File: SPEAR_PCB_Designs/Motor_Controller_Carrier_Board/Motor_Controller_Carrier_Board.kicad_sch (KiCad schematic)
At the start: 0 parts

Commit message: Added symbol for motor driver board and started the schematic
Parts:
- added F1, F2: Fuse, symbol Device:Fuse
- added J1, J2, J3: Conn_01x02_Pin, symbol Connector:Conn_01x02_Pin
- added MDB1: Motor_Driver_Board, Motor_Controller_Carrier_Board:Motor_Driver_Board, symbol Motor_Controller_Carrier_Board:Motor_Driver_Board
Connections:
- new net: J2.1 (Pin_1), MDB1.13 (OUTA), MDB1.14 (OUTA)
- new net: J2.2 (Pin_2), MDB1.11 (OUTB), MDB1.12 (OUTB)
- new net: J1.1 (Pin_1), J3.1 (Pin_1), MDB1.1 (GND), MDB1.10 (GND), MDB1.9 (GND)
- new net: F1.2, F2.1, J1.2 (Pin_2)
- new net: F2.2, MDB1.15 (VIN), MDB1.16 (VIN)
- new net: F1.1, J3.2 (Pin_2)

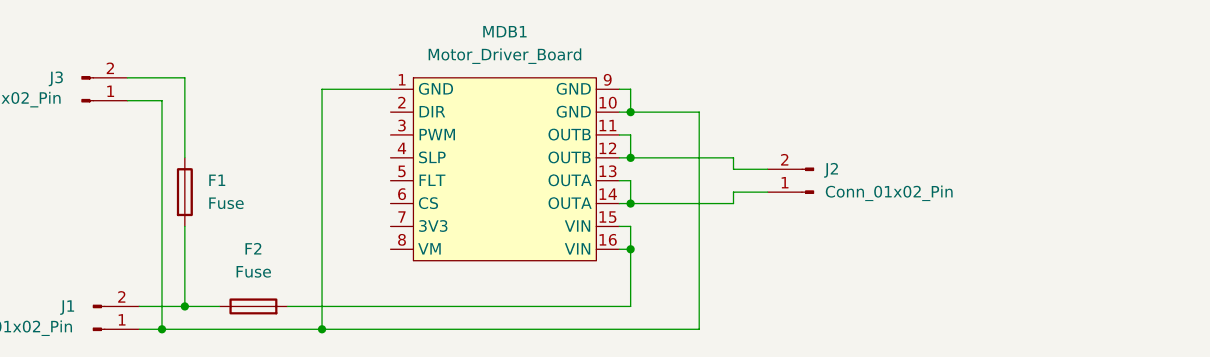
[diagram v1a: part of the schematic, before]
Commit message: Started Carrier Board PCB layout
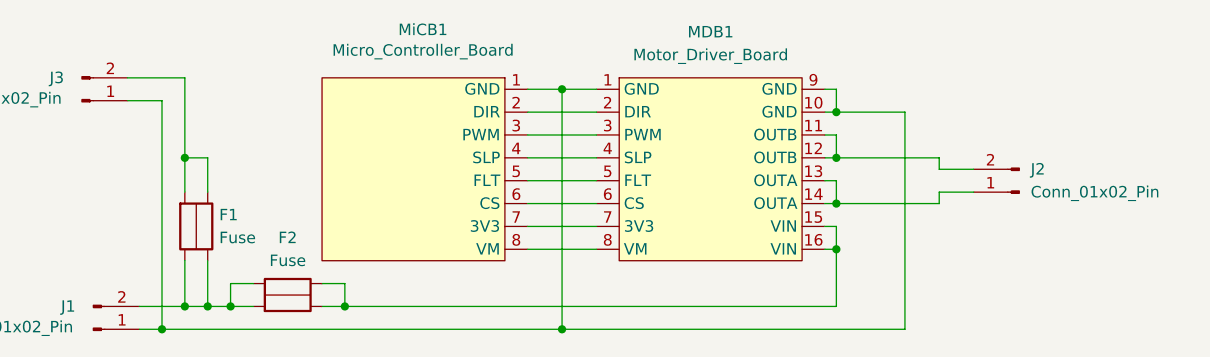
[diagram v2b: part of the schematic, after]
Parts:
- removed F1, F2: Fuse, symbol Device:Fuse
- added F1, F2: Fuse, Motor_Controller_Carrier_Board:Fuse, symbol Motor_Controller_Carrier_Board:Fuse
- added MiCB1: Micro_Controller_Board, Motor_Controller_Carrier_Board:Micro_Controller_Board, symbol Motor_Controller_Carrier_Board:Micro_Controller_Board
- J1, J2, J3: footprint (none) -> XT30:AMASS_XT30PW-M
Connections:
- net at J1.1 (Pin_1), J3.1 (Pin_1), MDB1.1 (GND)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: now also MiCB1.1 (GND)
- net at J1.2 (Pin_2): now also F1.2, F1.4, F2.1, F2.3
- net at MDB1.15 (VIN), MDB1.16 (VIN): now also F2.2, F2.4
- net at MDB1.2 (DIR): now also MiCB1.2 (DIR)
- net at MDB1.3 (PWM): now also MiCB1.3 (PWM)
- net at MDB1.4 (SLP): now also MiCB1.4 (SLP)
- net at MDB1.5 (FLT): now also MiCB1.5 (FLT)
- net at MDB1.6 (CS): now also MiCB1.6 (CS)
- net at MDB1.7 (3V3): now also MiCB1.7 (3V3)
- net at MDB1.8 (VM): now also MiCB1.8 (VM)
- net at J3.2 (Pin_2): now also F1.1, F1.3
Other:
- moved on the sheet: J2, MDB1

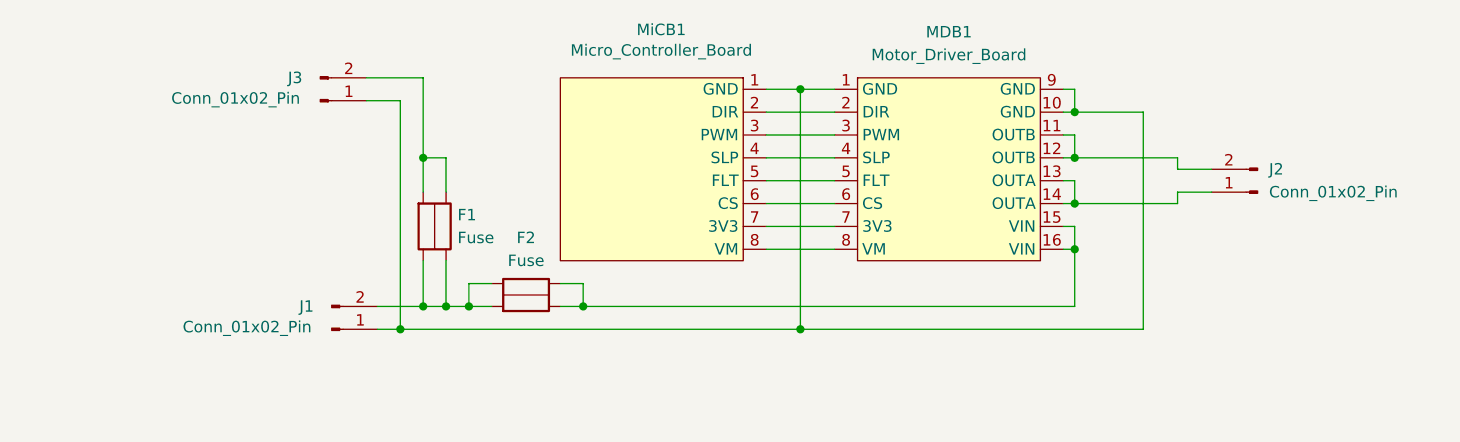
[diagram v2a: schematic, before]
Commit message: added Carrier Board PCB
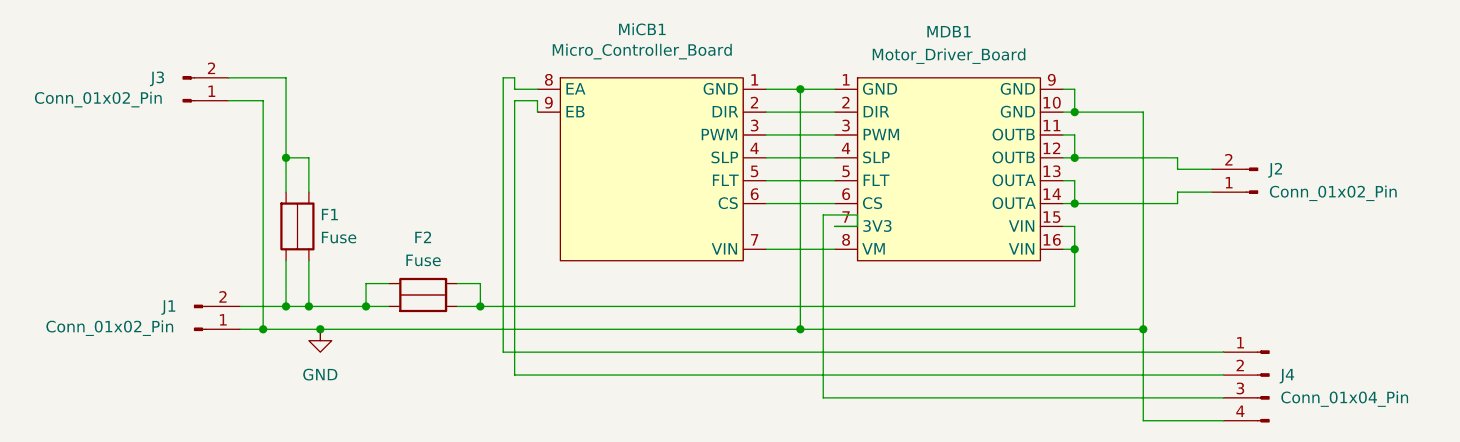
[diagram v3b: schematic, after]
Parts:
- added J4: Conn_01x04_Pin, Motor_Controller_Carrier_Board:JST_GH_BM04B-GHS-TBT_1x04-1MP_P1.25mm_Vertical, symbol Connector:Conn_01x04_Pin
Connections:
- net GND: now reaches J1.1 (Pin_1), J3.1 (Pin_1), MDB1.1 (GND), MDB1.10 (GND), MDB1.9 (GND), MiCB1.1 (GND)
- net GND: now also J4.4 (Pin_4)
- net at MiCB1.7 (VIN): now also MDB1.8 (VM); no longer MDB1.7 (3V3)
- net at MiCB1.8 (EA): now also J4.1 (Pin_1); no longer MDB1.8 (VM)
- new net: J4.2 (Pin_2), MiCB1.9 (EB)
- new net: J4.3 (Pin_3), MDB1.7 (3V3)
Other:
- moved on the sheet: F1, F2, J1, J3

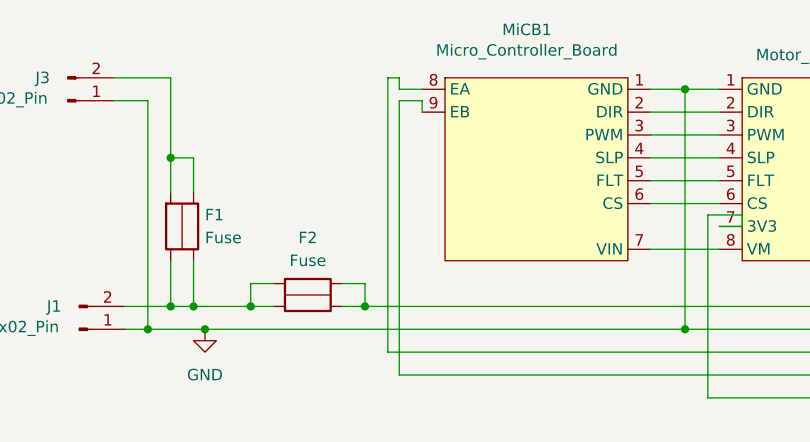
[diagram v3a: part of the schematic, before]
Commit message: moved board footprints and created new motor driver board footprints
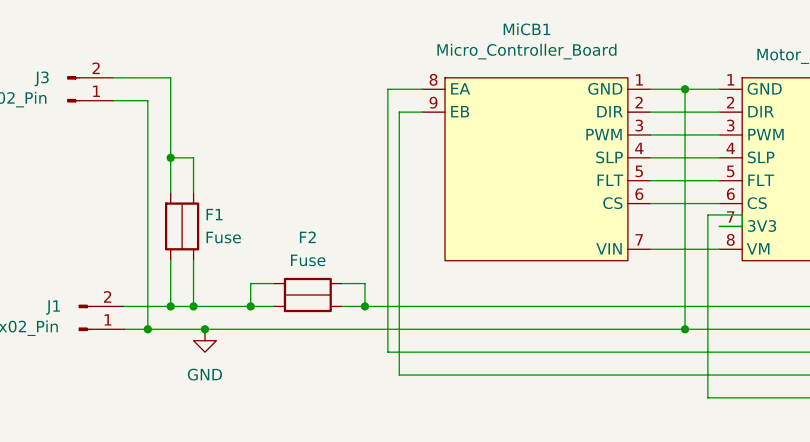
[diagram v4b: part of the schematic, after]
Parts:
- J1, J2, J3: footprint XT30:AMASS_XT30PW-M -> Connector_AMASS:AMASS_XT30PW-M_1x02_P2.50mm_Horizontal
- MDB1: footprint Motor_Controller_Carrier_Board:Motor_Driver_Board -> SPEAR_Boards:Motor_Driver_Board_2992
- MiCB1: footprint Motor_Controller_Carrier_Board:Micro_Controller_Board -> SPEAR_Boards:Micro_Controller_Board
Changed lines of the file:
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@@
 	(wire
 		(pts
-			(xy 116.84 88.9) (xy 119.38 88.9)
+			(xy 116.84 90.17) (xy 119.38 90.17)
 		)
 		(stroke
@@
 	(wire
 		(pts
-			(xy 119.38 88.9) (xy 119.38 90.17)
-		)
-		(stroke
-			(width 0)
-			(type default)
-		)
-	)
-	(wire
-		(pts
 			(xy 144.78 90.17) (xy 152.4 90.17)
 		)
@@
 	(wire
 		(pts
-			(xy 116.84 119.38) (xy 116.84 88.9)
+			(xy 116.84 119.38) (xy 116.84 90.17)
 		)
 		(stroke
@@
 	(wire
 		(pts
-			(xy 116.84 86.36) (xy 116.84 87.63)
-		)
-		(stroke
-			(width 0)
-			(type default)
-		)
-	)
-	(wire
-		(pts
 			(xy 177.8 87.63) (xy 179.07 87.63)
 		)
@@
 	(wire
 		(pts
-			(xy 116.84 87.63) (xy 119.38 87.63)
-		)
-		(stroke
-			(width 0)
-			(type default)
-		)
-	)
-	(wire
-		(pts
 			(xy 95.25 114.3) (xy 148.59 114.3)
 		)
@@
 	(wire
 		(pts
-			(xy 115.57 86.36) (xy 116.84 86.36)
+			(xy 115.57 87.63) (xy 119.38 87.63)
 		)
 		(stroke
@@
 	(wire
 		(pts
-			(xy 115.57 116.84) (xy 115.57 86.36)
+			(xy 115.57 116.84) (xy 115.57 87.63)
 		)
 		(stroke
@@
 			)
 		)
-		(property "Footprint" "XT30:AMASS_XT30PW-M"
+		(property "Footprint" "Connector_AMASS:AMASS_XT30PW-M_1x02_P2.50mm_Horizontal"
 			(at 199.39 99.06 0)
 			(effects
@@
 			)
 		)
-		(property "Footprint" "Motor_Controller_Carrier_Board:Micro_Controller_Board"
+		(property "Footprint" "SPEAR_Boards:Micro_Controller_Board"
 			(at 132.08 79.502 0)
 			(effects
@@
 			)
 		)
-		(property "Footprint" "XT30:AMASS_XT30PW-M"
+		(property "Footprint" "Connector_AMASS:AMASS_XT30PW-M_1x02_P2.50mm_Horizontal"
 			(at 81.28 114.3 0)
 			(effects
@@
 			)
 		)
-		(property "Footprint" "Motor_Controller_Carrier_Board:Motor_Driver_Board"
+		(property "Footprint" "SPEAR_Boards:Motor_Driver_Board_2992"
 			(at 165.1 74.168 0)
 			(effects
@@
 			)
 		)
-		(property "Footprint" "XT30:AMASS_XT30PW-M"
+		(property "Footprint" "Connector_AMASS:AMASS_XT30PW-M_1x02_P2.50mm_Horizontal"
 			(at 80.01 88.9 0)
 			(effects

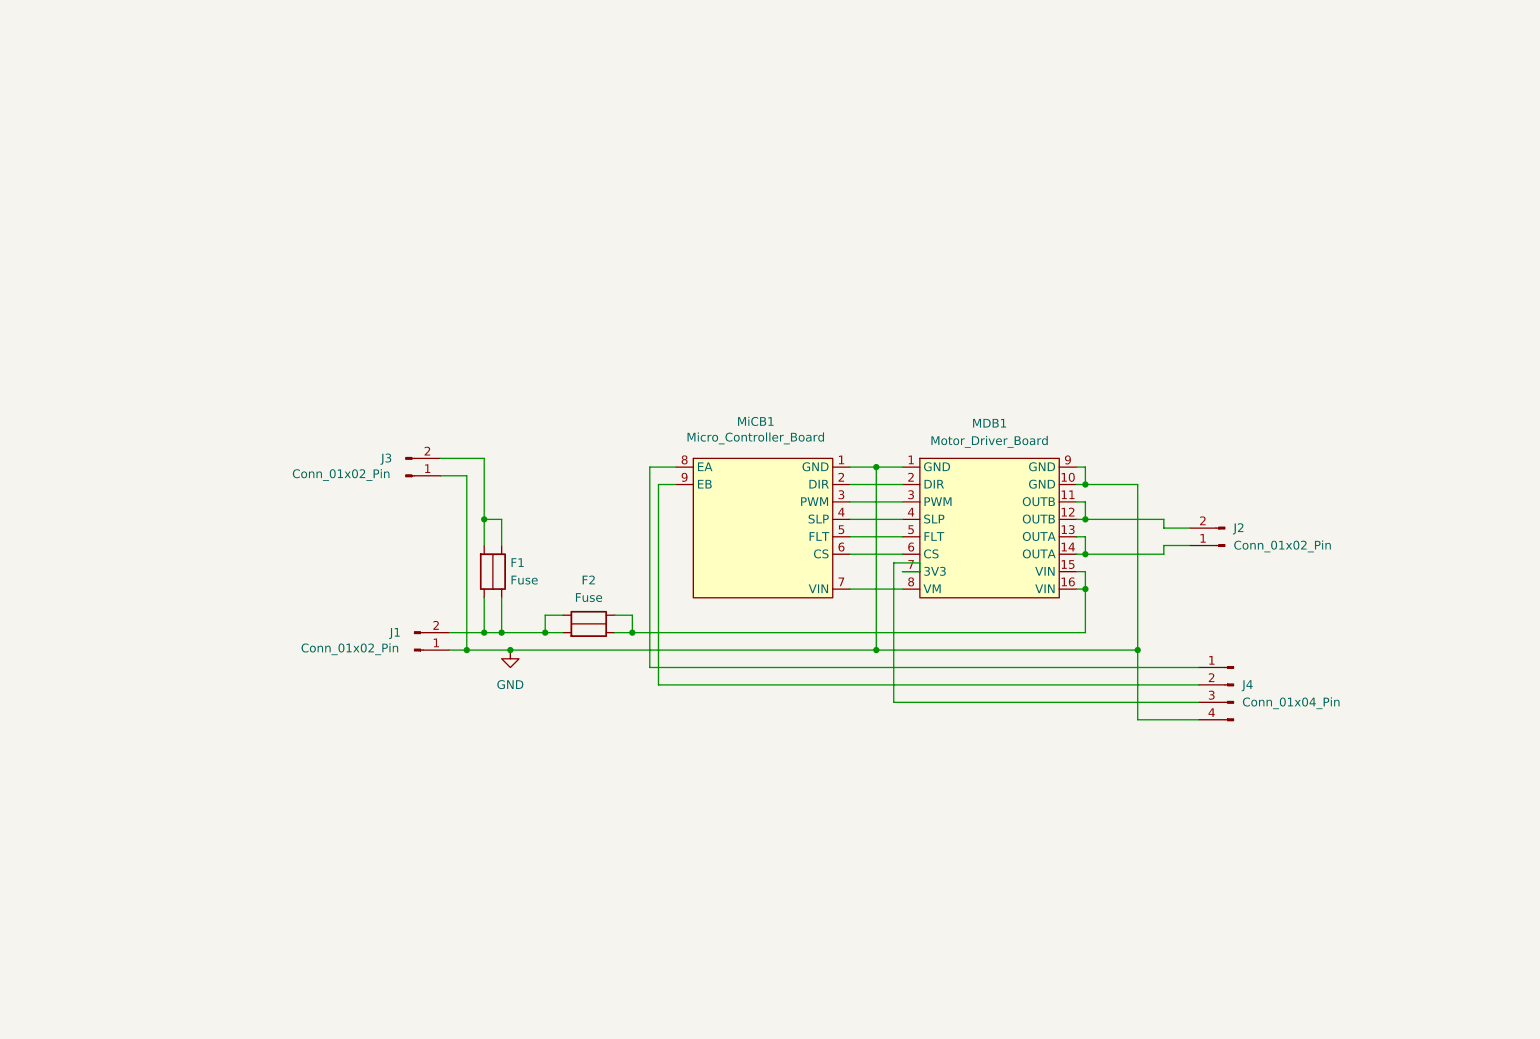
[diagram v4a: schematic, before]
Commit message: Created board symbols and added buck converter to carrier board
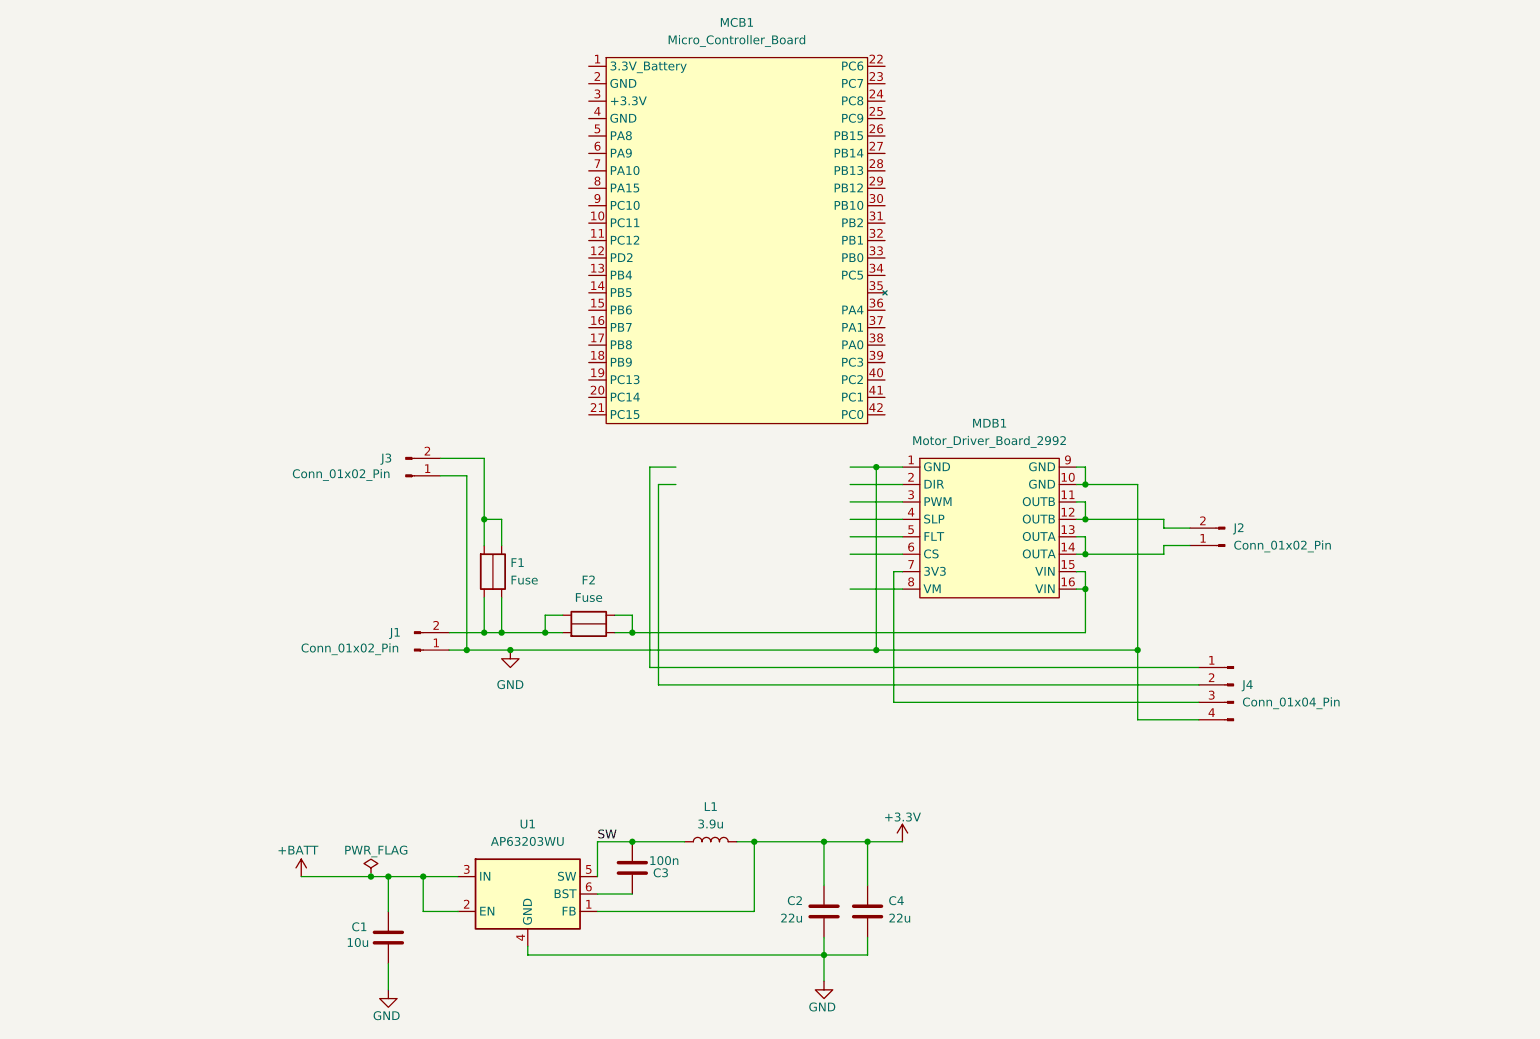
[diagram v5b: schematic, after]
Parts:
- removed MDB1: Motor_Driver_Board, SPEAR_Boards:Motor_Driver_Board_2992, symbol Motor_Controller_Carrier_Board:Motor_Driver_Board
- removed MiCB1: Micro_Controller_Board, SPEAR_Boards:Micro_Controller_Board, symbol Motor_Controller_Carrier_Board:Micro_Controller_Board
- added C1: 10u, AP63202Footprints:CAP_FG20_TDK_C1, symbol Device:C
- added C2, C4: 22u, AP63202Footprints:CAP_FG22_TDK_C2_C4, symbol Device:C
- added C3: 100n, Capacitor_THT:C_Disc_D5.0mm_W2.5mm_P5.00mm, symbol Device:C
- added L1: 3.9u, AP63202Footprints:L_Wurth_WE-LHMI-1040_L1, symbol Device:L
- added MCB1: Micro_Controller_Board, SPEAR_Boards:Micro_Controller_Board, symbol SPEAR_Boards:Micro_Controller_Board
- added MDB1: Motor_Driver_Board_2992, SPEAR_Boards:Motor_Driver_Board_2992, symbol SPEAR_Boards:Motor_Driver_Board_2992
- added U1: AP63203WU, Package_TO_SOT_SMD:TSOT-23-6, symbol Regulator_Switching:AP63203WU
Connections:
- net GND: now also C1.2, C2.2, C4.2, MDB1.1 (GND), MDB1.10 (GND), MDB1.9 (GND), U1.4 (GND)
- net at J2.1 (Pin_1): now also MDB1.13 (OUTA), MDB1.14 (OUTA)
- net at J2.2 (Pin_2): now also MDB1.11 (OUTB), MDB1.12 (OUTB)
- net at J4.3 (Pin_3): now also MDB1.7 (3V3)
- net at F2.2, F2.4: now also MDB1.15 (VIN), MDB1.16 (VIN)
- new net: C3.2, U1.6 (BST)
- new net +3.3V: C2.1, C4.1, L1.2, U1.1 (FB)
- new net +BATT: C1.1, U1.2 (EN), U1.3 (IN)
- new net SW: C3.1, L1.1, U1.5 (SW)

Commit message: Finished schematic and general PCB layout for carrier board 2992
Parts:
- removed F1, F2: Fuse, Motor_Controller_Carrier_Board:Fuse, symbol Motor_Controller_Carrier_Board:Fuse
- removed J4: Conn_01x04_Pin, Motor_Controller_Carrier_Board:JST_GH_BM04B-GHS-TBT_1x04-1MP_P1.25mm_Vertical, symbol Connector:Conn_01x04_Pin
- added C5: C, Motor_Controller_Carrier_Board:CAP_UBY_18X20_NCH, symbol Device:C
- added F1, F2: 3557-10, Motor_Controller_Carrier_Board:FUSE_3557-10, symbol Motor_Controller_Carrier_Board:3557-10
- added J4: JST_S4B-XH-A-1, Connector_JST:JST_XH_S4B-XH-A-1_1x04_P2.50mm_Horizontal, symbol Motor_Controller_Carrier_Board:JST_S4B-XH-A-1
- C1: footprint AP63202Footprints:CAP_FG20_TDK_C1 -> SPEAR_AP63203BuckConverter:CAP_FG20_TDK_C1
- C2, C4: footprint AP63202Footprints:CAP_FG22_TDK_C2_C4 -> SPEAR_AP63203BuckConverter:CAP_FG22_TDK_C2_C4
- L1: footprint AP63202Footprints:L_Wurth_WE-LHMI-1040_L1 -> SPEAR_AP63203BuckConverter:L_Wurth_WE-LHMI-1040_L1
- renumbered J3 to J2, J2 to J3
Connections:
- net +3.3V: now also MCB1.1 (3.3V_Battery), J4.4 (VCC)
- net +BATT: now also MDB1.15 (VIN), MDB1.16 (VIN), C5.1, F1.2_1, F1.2_2
- net GND: now also MCB1.2 (GND), MCB1.4 (GND), C5.2, J4.3 (GND)
- net DIR: now reaches MDB1.2 (DIR)
- net DIR: now also MCB1.21 (PC6)
- net PWM: now reaches MDB1.3 (PWM)
- net PWM: now also MCB1.22 (PC7)
- net SLP: now reaches MDB1.4 (SLP)
- net SLP: now also MCB1.23 (PC8)
- net FLT: now reaches MDB1.5 (FLT)
- net FLT: now also MCB1.24 (PC9)
- net CS: now reaches MDB1.6 (CS)
- net CS: now also MCB1.31 (PB1)
- net at J1.2 (Pin_2): now also F1.1_1, F1.1_2, F2.1_1, F2.1_2
- net at J2.2 (Pin_2): now also F2.2_1, F2.2_2
- net ENC_B: now reaches MCB1.35 (PA1)
- net ENC_B: now also MCB1.36 (PA0), J4.1 (B)
- net ENC_A: now reaches MCB1.8 (PA15)
- net ENC_A: now also J4.2 (A)
- no-connect marks 0 -> 31
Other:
- company: (none) -> SPEAR
- title: (none) -> Motor Controller Carrier Board
- moved on the sheet: C1, C2, C3, C4, J1, J2, J3, L1, U1

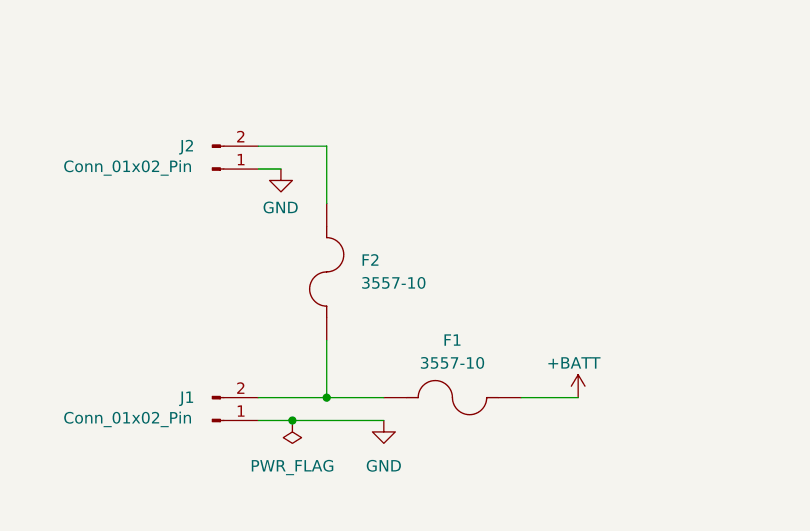
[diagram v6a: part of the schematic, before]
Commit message: Added silkscreen and courtyards to board footprints and 3D models to the carrier board
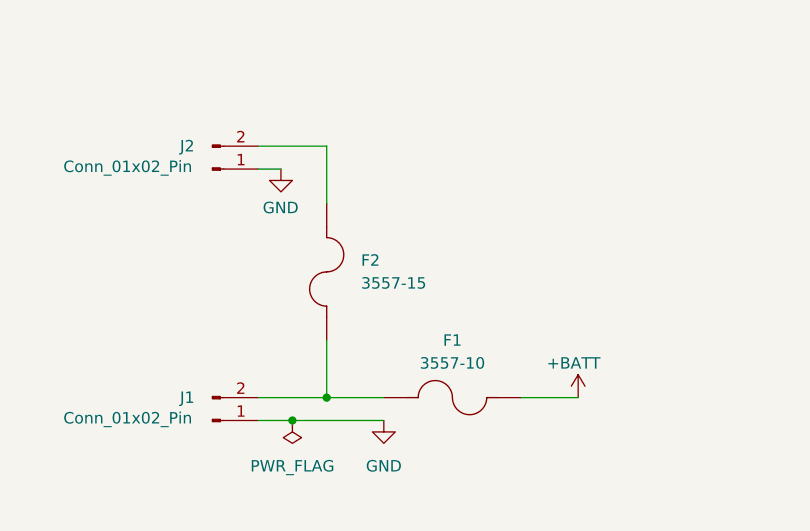
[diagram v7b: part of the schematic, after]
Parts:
- F2: value 3557-10 -> 3557-15; footprint Motor_Controller_Carrier_Board:FUSE_3557-10 -> Motor_Controller_Carrier_Board:FUSE_3557-15
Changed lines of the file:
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@@
 			)
 		)
-		(property "Value" "3557-10"
+		(property "Value" "3557-15"
 			(at 93.98 129.5399 90)
 			(effects
@@
 			)
 		)
-		(property "Footprint" "Motor_Controller_Carrier_Board:FUSE_3557-10"
+		(property "Footprint" "Motor_Controller_Carrier_Board:FUSE_3557-15"
 			(at 82.042 128.27 0)
 			(effects
